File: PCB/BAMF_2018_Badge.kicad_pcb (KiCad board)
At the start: 2 copper layers, 73.4 x 87.2 mm, 14 parts, among them J1 Conn_01x02, SW1 RED, SW2 GREEN, SW3 BLUE, SW4 YELLOW, U1 BAMF_2018_Badge

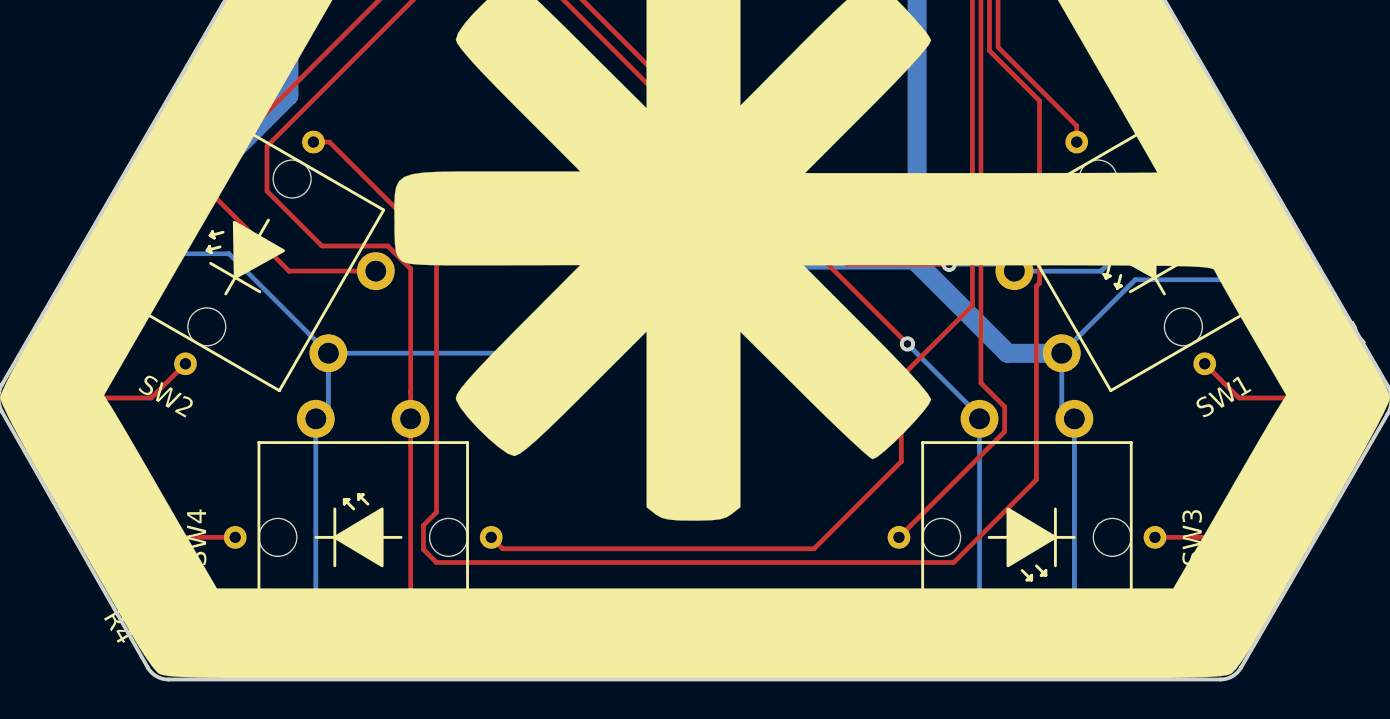
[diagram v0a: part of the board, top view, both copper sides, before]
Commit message: Adding final silk
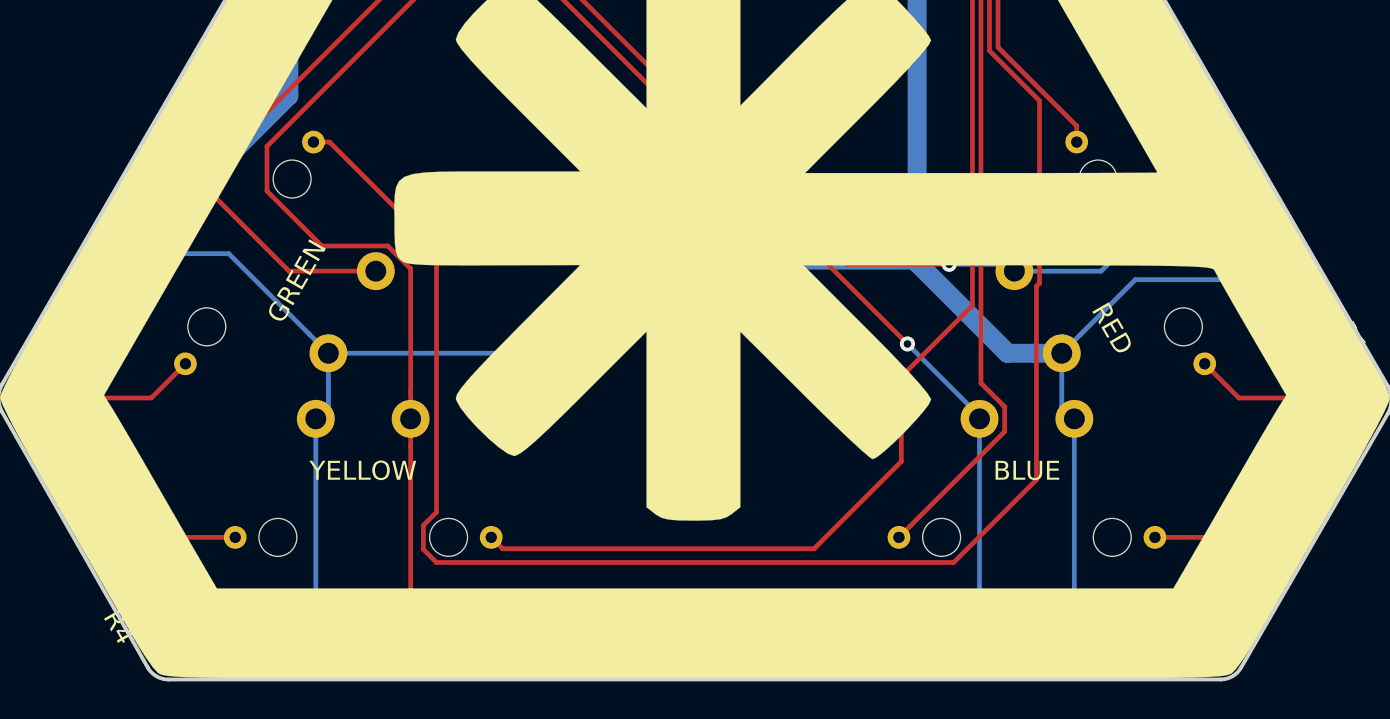
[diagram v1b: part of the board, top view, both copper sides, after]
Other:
- board text added: "Bay Area Maker Faire 2018"
- board text added: "Hold RED + GREEN to Start"
- board text added: "Maniacal Labs"
